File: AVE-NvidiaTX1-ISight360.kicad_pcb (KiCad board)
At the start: 2 copper layers, 104.1 x 106.7 mm, 48 parts, among them P301 CONN_02X20, P401 CONN_01X04, P402 CONN_01X04, P501 Ultrasonic 1, P502 Ultrasonic2, P503 Ultrasonic3, P504 Ultrasonic4, P505 Ultrasonic5, P506 Ultrasonic6, U201 TPS54231DR, U401 74LVC1T45, U402 74LVC1T45, U403 74LVC1T45, U404 CD4051B, U405 DRV2605L(breakout), U406 DRV2605L(breakout), U407 DRV2605L(breakout), U408 DRV2605L(breakout), U409 DRV2605L(breakout), U410 DRV2605L(breakout), U501 74LVC1T45, U502 74LS251

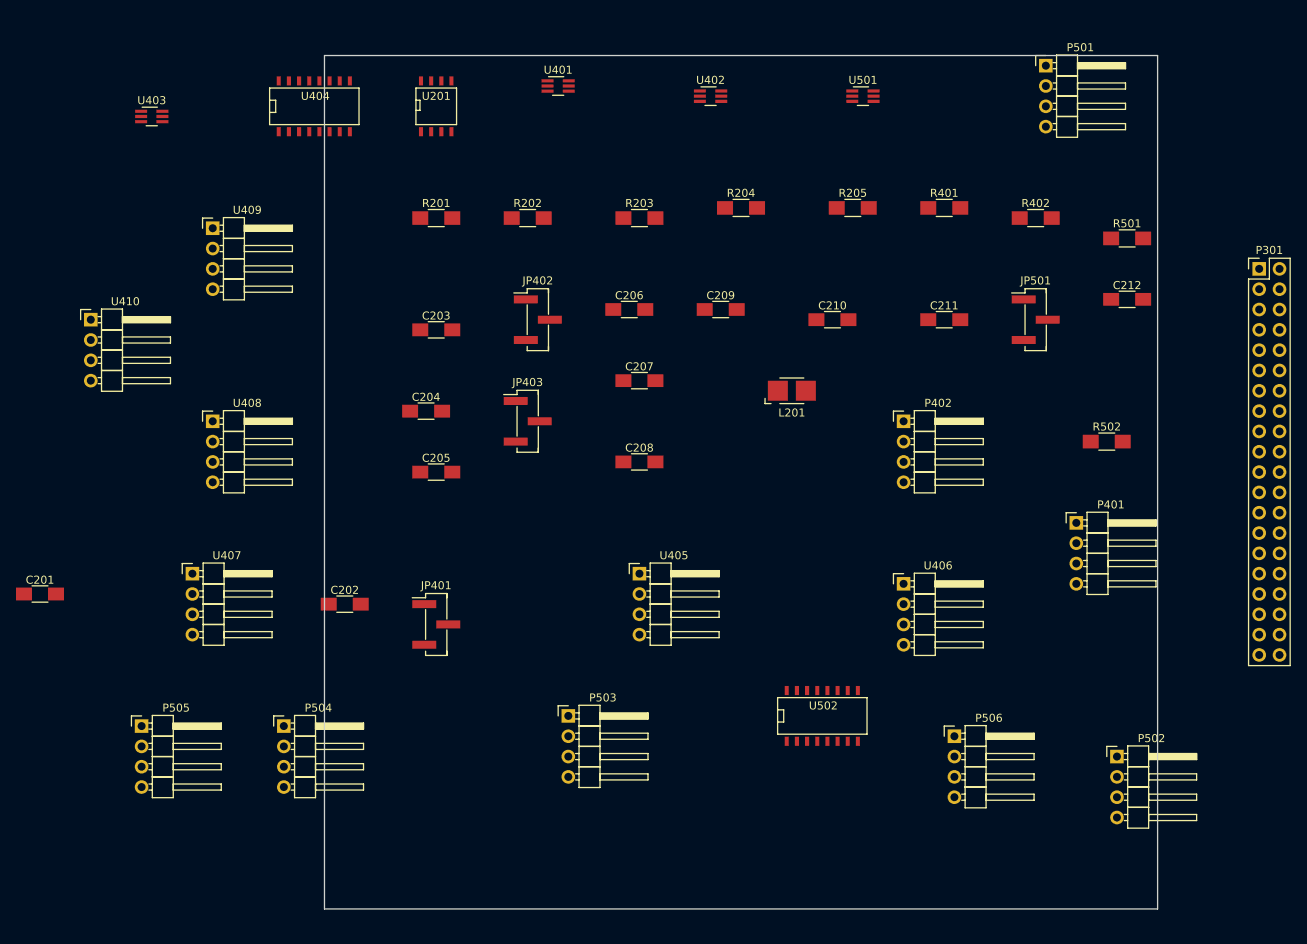
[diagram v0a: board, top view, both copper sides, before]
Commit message: Reduced number of components
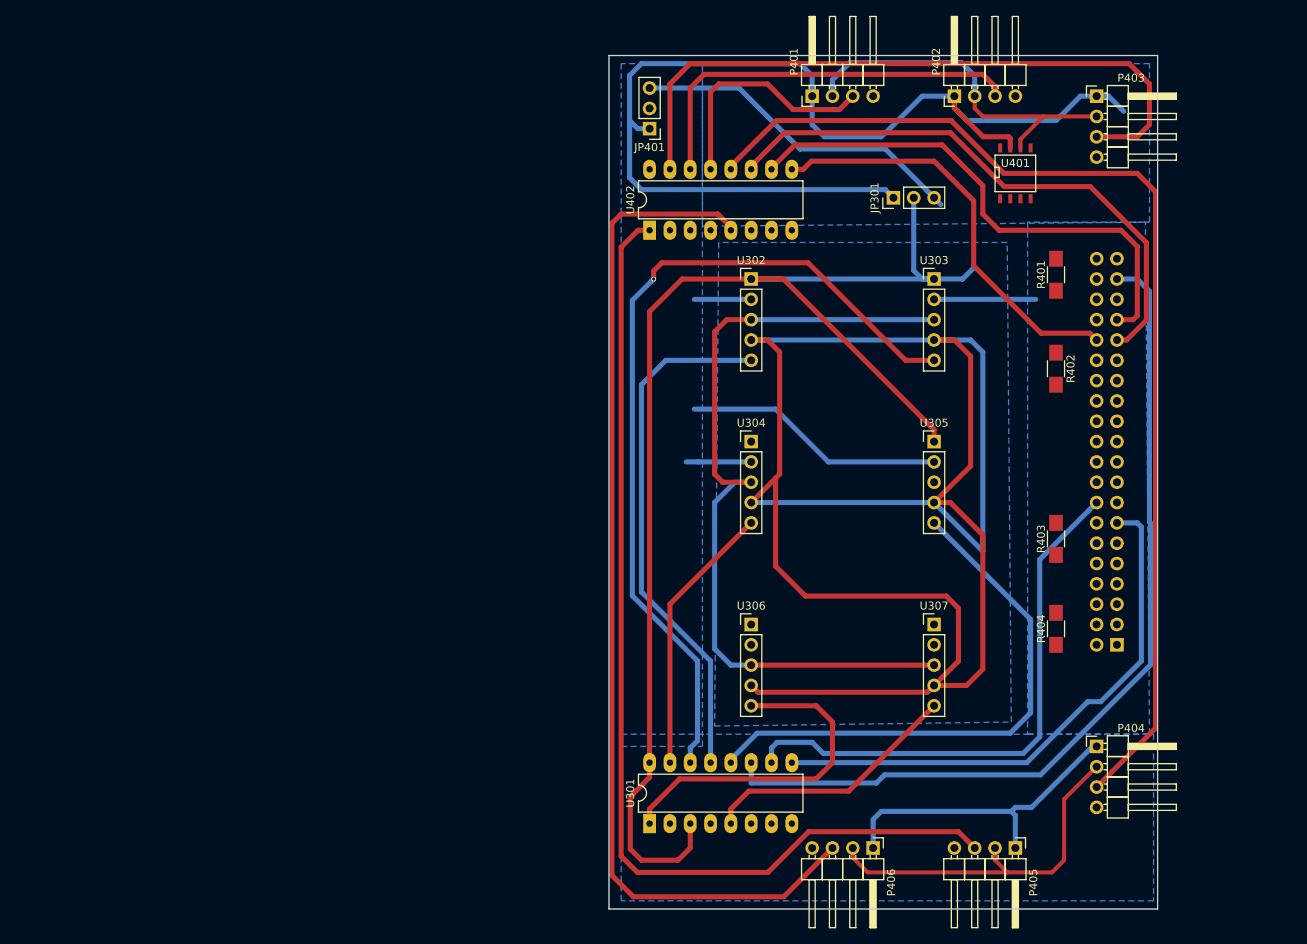
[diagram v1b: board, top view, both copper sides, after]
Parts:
- removed C201: 10uF, Capacitors_SMD:C_1206_HandSoldering
- removed C202: 100uF, Capacitors_SMD:C_1206_HandSoldering
- removed C203, C208: .1uF, Capacitors_SMD:C_1206_HandSoldering
- removed C204, C205, C206: 4.7uF, Capacitors_SMD:C_1206_HandSoldering
- removed C207: .015uF, Capacitors_SMD:C_1206_HandSoldering
- removed C209: 1000pF, Capacitors_SMD:C_1206_HandSoldering
- removed C210, C212: 47uF, Capacitors_SMD:C_1206_HandSoldering
- removed C211: 47pF, Capacitors_SMD:C_1206_HandSoldering
- removed JP402: CTRL Jump2, Pin_Headers:Pin_Header_Straight_1x03_Pitch2.54mm_SMD_Pin1Left
- removed JP403: CTRL Jump3, Pin_Headers:Pin_Header_Straight_1x03_Pitch2.54mm_SMD_Pin1Left
- removed JP501: Jumper_NC_Dual, Pin_Headers:Pin_Header_Straight_1x03_Pitch2.54mm_SMD_Pin1Left
- removed L201: 10uH, Inductors:Inductor_1212
- removed P301: CONN_02X20, Pin_Headers:Pin_Header_Straight_2x20_Pitch2.54mm
- removed P501: Ultrasonic 1, Pin_Headers:Pin_Header_Angled_1x04_Pitch2.54mm
- removed P502: Ultrasonic2, Pin_Headers:Pin_Header_Angled_1x04_Pitch2.54mm
- removed P503: Ultrasonic3, Pin_Headers:Pin_Header_Angled_1x04_Pitch2.54mm
- removed P504: Ultrasonic4, Pin_Headers:Pin_Header_Angled_1x04_Pitch2.54mm
- removed P505: Ultrasonic5, Pin_Headers:Pin_Header_Angled_1x04_Pitch2.54mm
- removed P506: Ultrasonic6, Pin_Headers:Pin_Header_Angled_1x04_Pitch2.54mm
- removed R201: 332k, Resistors_SMD:R_1206_HandSoldering
- removed R202: 68.1k, Resistors_SMD:R_1206_HandSoldering
- removed R203: 29.4k, Resistors_SMD:R_1206_HandSoldering
- removed R204: 10.2k, Resistors_SMD:R_1206_HandSoldering
- removed R205: R_Small, Resistors_SMD:R_1206_HandSoldering
- removed R501, R502: 10K, Resistors_SMD:R_1206_HandSoldering
- removed U201: TPS54231DR, SMD_Packages:SOIC-8-N
- removed U403, U501: 74LVC1T45, TO_SOT_Packages_SMD:SOT-363_SC-70-6_Handsoldering
- removed U404: CD4051B, SMD_Packages:SO-16-N
- removed U405, U406, U407, U408, U409, U410: DRV2605L(breakout), Pin_Headers:Pin_Header_Angled_1x04_Pitch2.54mm
- removed U502: 74LS251, SMD_Packages:SO-16-N
- added JP301: Motor Power Select, Pin_Headers:Pin_Header_Straight_1x03_Pitch2.54mm, F.Cu at (147.3, 53.3)
- added P201: CONN_02X20, Socket_Strips:Socket_Strip_Straight_2x20_Pitch2.54mm, B.Cu at (175.3, 109.2)
- added P403: Ultrasonic3, Pin_Headers:Pin_Header_Angled_1x04_Pitch2.54mm, F.Cu at (172.7, 40.6)
- added P404: Ultrasonic4, Pin_Headers:Pin_Header_Angled_1x04_Pitch2.54mm, F.Cu at (172.7, 121.9)
- added P405: Ultrasonic5, Pin_Headers:Pin_Header_Angled_1x04_Pitch2.54mm, F.Cu at (162.6, 134.6)
- added P406: Ultrasonic6, Pin_Headers:Pin_Header_Angled_1x04_Pitch2.54mm, F.Cu at (144.8, 134.6)
- added R403: 100K, Resistors_SMD:R_1206_HandSoldering, F.Cu at (167.6, 96.0)
- added R404: 10K, Resistors_SMD:R_1206_HandSoldering, F.Cu at (167.6, 107.2)
- added U301: CD4051B, Housings_DIP:DIP-16_W7.62mm_LongPads, F.Cu at (116.8, 131.6)
- added U302: DRV2605L(breakout), Socket_Strips:Socket_Strip_Straight_1x05_Pitch2.54mm, F.Cu at (129.5, 63.5)
- added U303: DRV2605L(breakout), Socket_Strips:Socket_Strip_Straight_1x05_Pitch2.54mm, F.Cu at (152.4, 63.5)
- added U304: DRV2605L(breakout), Socket_Strips:Socket_Strip_Straight_1x05_Pitch2.54mm, F.Cu at (129.5, 83.8)
- added U305: DRV2605L(breakout), Socket_Strips:Socket_Strip_Straight_1x05_Pitch2.54mm, F.Cu at (152.4, 83.8)
- added U306: DRV2605L(breakout), Socket_Strips:Socket_Strip_Straight_1x05_Pitch2.54mm, F.Cu at (129.5, 106.7)
- added U307: DRV2605L(breakout), Socket_Strips:Socket_Strip_Straight_1x05_Pitch2.54mm, F.Cu at (152.4, 106.7)
- JP401: value CTRL Jump1 -> Usonic Power Select; footprint Pin_Headers:Pin_Header_Straight_1x03_Pitch2.54mm_SMD_Pin1Left -> Pin_Headers:Pin_Header_Straight_1x03_Pitch2.54mm
- P401: value CONN_01X04 -> Ultrasonic 1
- P402: value CONN_01X04 -> Ultrasonic2
- R401: value 33 -> 10K
- R402: value 33 -> 20K
- U401: value 74LVC1T45 -> LM4250; footprint TO_SOT_Packages_SMD:SOT-363_SC-70-6_Handsoldering -> SMD_Packages:SOIC-8-N
- U402: value 74LVC1T45 -> CD4051B; footprint TO_SOT_Packages_SMD:SOT-363_SC-70-6_Handsoldering -> Housings_DIP:DIP-16_W7.62mm_LongPads
- moved JP401 67.5 mm to (116.8, 44.7), turned to 180 degrees
- moved P401 62.7 mm to (137.2, 40.6), turned to 90 degrees
- moved U401 58.2 mm to (162.6, 50.3)
- moved P402 41.1 mm to (154.9, 40.6), turned to 90 degrees
- moved R402 19.0 mm to (167.6, 74.7), turned to 270 degrees
- moved U402 18.4 mm to (116.8, 57.4), turned to 90 degrees
- moved R401 16.3 mm to (167.6, 63.0), turned to 90 degrees
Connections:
- JP401 pad 1: /GPIO Breakout/GPIO38 -> /GPIO Breakout/5V
- JP401 pad 2: Net-(JP401-Pad2) -> /UltrasonicSensorBank/U-Power
- JP401 pad 3: Net-(JP401-Pad3) -> /GPIO Breakout/3.3V
- P401 pad 1: +5F -> /GPIO Breakout/5V
- P401 pad 2: /SDA -> /UltrasonicSensorBank/Ultrasonic_Trigger
- P401 pad 3: /SCL -> /UltrasonicSensorBank/Echo1
- P402 pad 1: +5F -> /GPIO Breakout/5V
- P402 pad 2: Net-(P402-Pad2) -> /UltrasonicSensorBank/Ultrasonic_Trigger
- P402 pad 3: Net-(P402-Pad3) -> /UltrasonicSensorBank/Echo2
- R401 pad 1: GND -> /Sensor_Input_Val
- R401 pad 2: Net-(P402-Pad2) -> Net-(R401-Pad2)
- R402 pad 1: GND -> /Sensor_Input_Val
- R402 pad 2: Net-(P402-Pad3) -> GND
- U401 pad 1: +5F -> Net-(U401-Pad1)
- U401 pad 2: GND -> Net-(R403-Pad2)
- U401 pad 3: Net-(JP402-Pad3) -> /Sensor_Trigger
- U401 pad 4: /GPIO Breakout/GPIO37 -> GND
- U401 pad 5: GND -> Net-(U401-Pad5)
- U401 pad 6: (no net) -> /UltrasonicSensorBank/Ultrasonic_Trigger
- U402 pad 1: +5F -> /UltrasonicSensorBank/Echo5
- U402 pad 2: GND -> Net-(U402-Pad2)
- U402 pad 3: Net-(JP401-Pad3) -> Net-(R401-Pad2)
- U402 pad 4: /GPIO Breakout/GPIO38 -> Net-(U402-Pad4)
- U402 pad 5: GND -> /UltrasonicSensorBank/Echo6
- U402 pad 6: (no net) -> Net-(U402-Pad6)
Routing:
- net /SDA: track 0.00 -> 238.0 mm
- net /GPIO Breakout/5V: track 0.00 -> 177.1 mm
- net /HapticMotorBank/M-Power: track 0.00 -> 167.1 mm
- net /UltrasonicSensorBank/Echo4: track 0.00 -> 137.0 mm
- net /UltrasonicSensorBank/Echo6: track 0.00 -> 129.1 mm
- net /UltrasonicSensorBank/Echo5: track 0.00 -> 128.5 mm
- net /GPIO Breakout/GPIO187: track 0.00 -> 110.0 mm
- net Net-(U301-Pad14): track 0.00 -> 106.9 mm, vias 0 -> 1
- net /SCL: track 0.00 -> 103.0 mm
- net /UltrasonicSensorBank/Ultrasonic_Trigger: track 0.00 -> 92.3 mm
- net /UltrasonicSensorBank/Echo3: track 0.00 -> 85.0 mm
- net /GPIO Breakout/GPIO186: track 0.00 -> 71.6 mm
- net /GPIO Breakout/GPIO37: track 0.00 -> 69.3 mm
- net Net-(U301-Pad12): track 0.00 -> 69.0 mm
- net /GPIO Breakout/GPIO38: track 0.00 -> 69.0 mm
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- added copper zone on B.Cu, net /HapticMotorBank/M-Power
- added copper zone on B.Cu, net GND
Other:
- board size 104.1 x 106.7 mm -> 68.6 x 106.7 mm
- net class Default: clearance 0.2 -> 0.508; trace_width 0.25 -> 0.508
- net class Larger added: clearance 0.508, trace_width 0.635, via_dia 0.6, via_drill 0.4
- net class Largest added: clearance 0.508, trace_width 7.62, via_dia 0.6, via_drill 0.4
- rule trace_clearance: 0.2 -> 0.508
- rule trace_min: 0.2 -> 0.381
